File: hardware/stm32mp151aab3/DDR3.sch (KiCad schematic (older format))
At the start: 14 parts

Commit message: update
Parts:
- added C? (x6): 100n, symbol Device:C_Small
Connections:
- net GND: now also C?.2, C?.2, C?.2, C?.2, C?.2, C?.2
- net VDD_DDR: now also C?.1, C?.1, C?.1, C?.1, C?.1, C?.1
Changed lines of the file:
@@
 $Descr A4 11693 8268
 encoding utf-8
-Sheet 6 6
+Sheet 6 7
 Title ""
 Date ""
@@
 Wire Wire Line
 	4350 6600 4350 6800
+Text Label 1350 750  0    50   ~ 0
+DDR_SIGNALS
+$Comp
+L Device:C_Small C?
+U 1 1 6021DB1E
+P 7600 2250
+F 0 "C?" H 7692 2296 50  0000 L CNN
+F 1 "100n" H 7692 2205 50  0000 L CNN
+F 2 "" H 7600 2250 50  0001 C CNN
+F 3 "~" H 7600 2250 50  0001 C CNN
+	1    7600 2250
+	1    0    0    -1
+$EndComp
+$Comp
+L Device:C_Small C?
+U 1 1 6021DB28
+P 8000 2250
+F 0 "C?" H 8092 2296 50  0000 L CNN
+F 1 "100n" H 8092 2205 50  0000 L CNN
+F 2 "" H 8000 2250 50  0001 C CNN
+F 3 "~" H 8000 2250 50  0001 C CNN
+	1    8000 2250
+	1    0    0    -1
+$EndComp
+$Comp
+L Device:C_Small C?
+U 1 1 6021DB32
+P 8400 2250
+F 0 "C?" H 8492 2296 50  0000 L CNN
+F 1 "100n" H 8492 2205 50  0000 L CNN
+F 2 "" H 8400 2250 50  0001 C CNN
+F 3 "~" H 8400 2250 50  0001 C CNN
+	1    8400 2250
+	1    0    0    -1
+$EndComp
+$Comp
+L Device:C_Small C?
+U 1 1 6021DB3C
+P 8800 2250
+F 0 "C?" H 8892 2296 50  0000 L CNN
+F 1 "100n" H 8892 2205 50  0000 L CNN
+F 2 "" H 8800 2250 50  0001 C CNN
+F 3 "~" H 8800 2250 50  0001 C CNN
+	1    8800 2250
+	1    0    0    -1
+$EndComp
+$Comp
+L Device:C_Small C?
+U 1 1 6021DB46
+P 9200 2250
+F 0 "C?" H 9292 2296 50  0000 L CNN
+F 1 "100n" H 9292 2205 50  0000 L CNN
+F 2 "" H 9200 2250 50  0001 C CNN
+F 3 "~" H 9200 2250 50  0001 C CNN
+	1    9200 2250
+	1    0    0    -1
+$EndComp
+$Comp
+L Device:C_Small C?
+U 1 1 6021DB50
+P 9600 2250
+F 0 "C?" H 9692 2296 50  0000 L CNN
+F 1 "100n" H 9692 2205 50  0000 L CNN
+F 2 "" H 9600 2250 50  0001 C CNN
+F 3 "~" H 9600 2250 50  0001 C CNN
+	1    9600 2250
+	1    0    0    -1
+$EndComp
+Wire Wire Line
+	9600 2150 9600 2100
+Wire Wire Line
+	7200 2100 7600 2100
+$Comp
+L power:GND #PWR?
+U 1 1 6021DB5C
+P 7600 2450
+F 0 "#PWR?" H 7600 2200 50  0001 C CNN
+F 1 "GND" H 7605 2277 50  0000 C CNN
+F 2 "" H 7600 2450 50  0001 C CNN
+F 3 "" H 7600 2450 50  0001 C CNN
+	1    7600 2450
+	1    0    0    -1
+$EndComp
+Wire Wire Line
+	7600 2350 7600 2400
+Wire Wire Line
+	7600 2400 8000 2400
+Wire Wire Line
+	9600 2400 9600 2350
+Connection ~ 7600 2400
+Wire Wire Line
+	7600 2400 7600 2450
+Wire Wire Line
+	9200 2350 9200 2400
+Connection ~ 9200 2400
+Wire Wire Line
+	9200 2400 9600 2400
+Wire Wire Line
+	8000 2350 8000 2400
+Connection ~ 8000 2400
+Wire Wire Line
+	8000 2400 8400 2400
+Wire Wire Line
+	8400 2350 8400 2400
+Connection ~ 8400 2400
+Wire Wire Line
+	8400 2400 8800 2400
+Wire Wire Line
+	8800 2350 8800 2400
+Connection ~ 8800 2400
+Wire Wire Line
+	8800 2400 9200 2400
+Wire Wire Line
+	7600 2150 7600 2100
+Connection ~ 7600 2100
+Wire Wire Line
+	7600 2100 8000 2100
+Wire Wire Line
+	8000 2150 8000 2100
+Connection ~ 8000 2100
+Wire Wire Line
+	8000 2100 8400 2100
+Wire Wire Line
+	8400 2150 8400 2100
+Connection ~ 8400 2100
+Wire Wire Line
+	8400 2100 8800 2100
+Wire Wire Line
+	8800 2150 8800 2100
+Connection ~ 8800 2100
+Wire Wire Line
+	8800 2100 9200 2100
+Wire Wire Line
+	9200 2150 9200 2100
+Connection ~ 9200 2100
+Wire Wire Line
+	9200 2100 9600 2100
+Wire Wire Line
+	7200 1450 7200 2100
 Wire Bus Line
 	2000 750  2000 6350
+Connection ~ 7200 1450
 $EndSCHEMATC

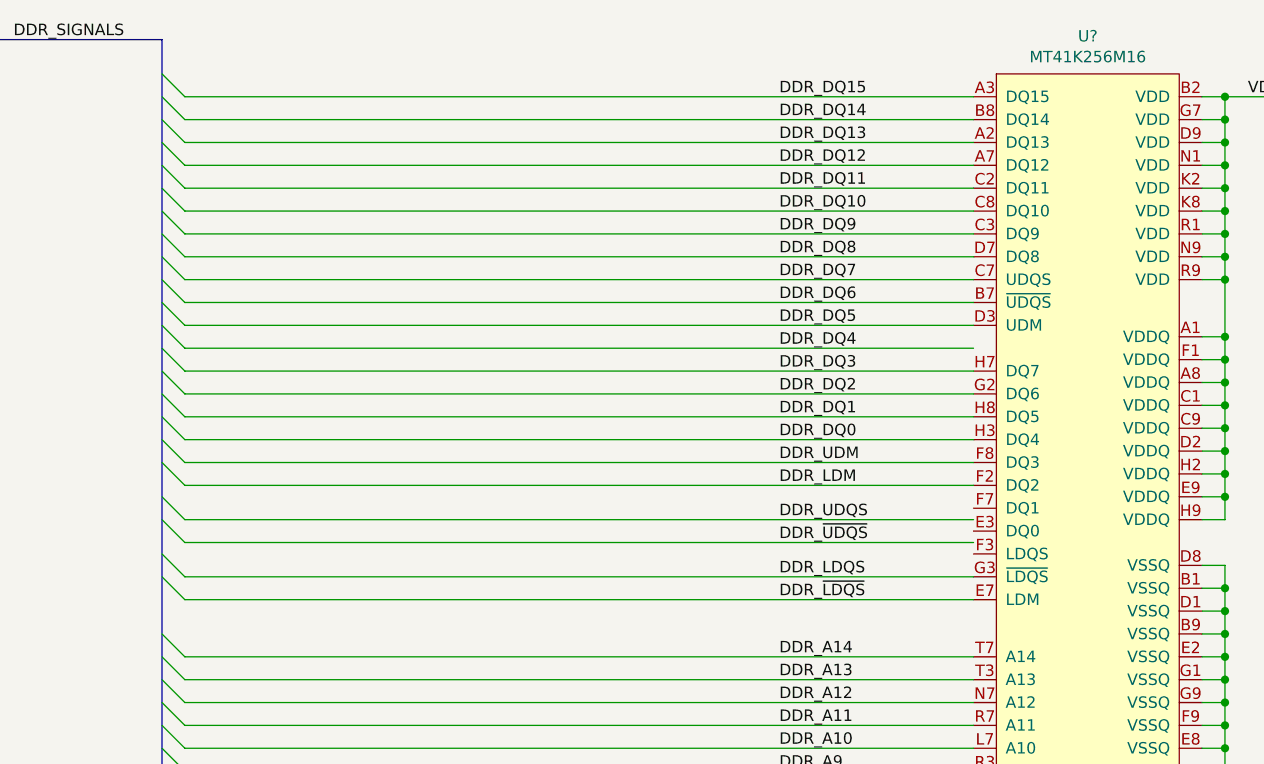
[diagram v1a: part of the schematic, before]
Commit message: update schematic and pdf
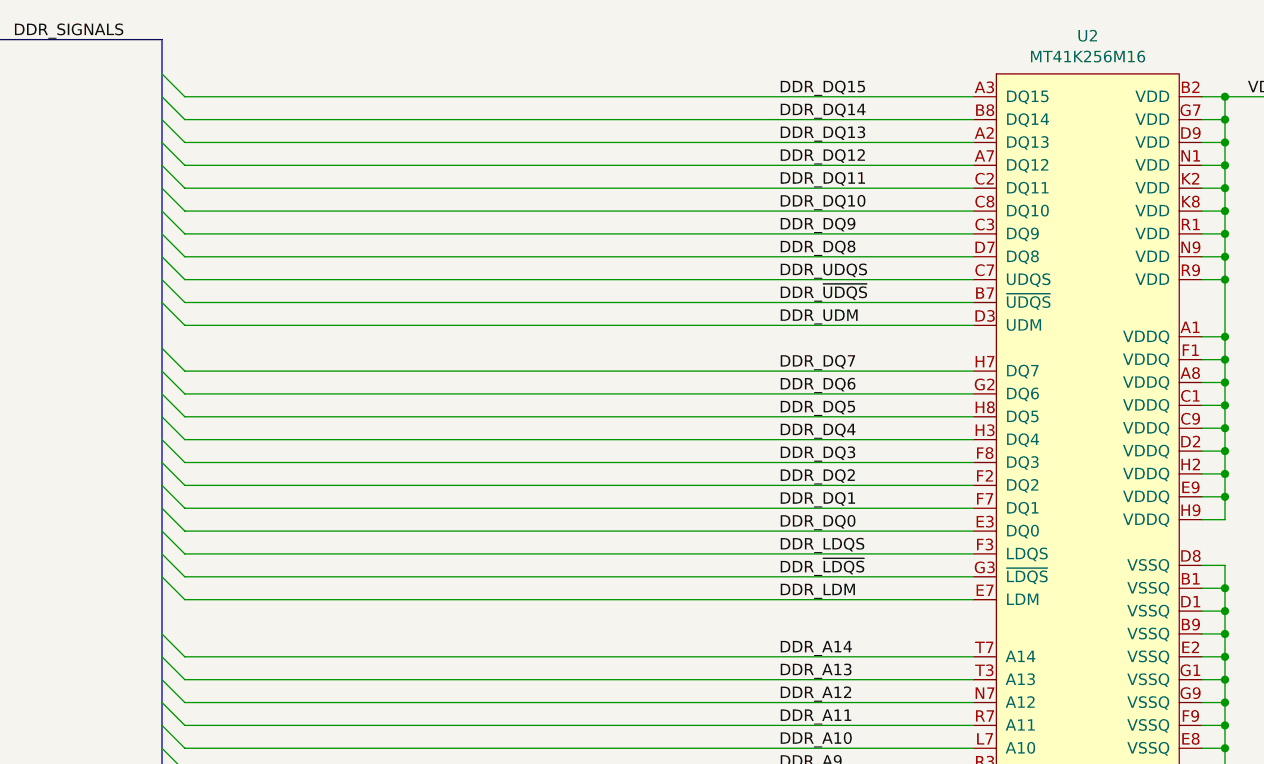
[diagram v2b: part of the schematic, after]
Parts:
- gave numbers to parts that had none: 1
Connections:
- net DDR_DQ0: now also U2.E3 (DQ0); no longer U2.H3 (DQ4)
- net DDR_DQ1: now also U2.F7 (DQ1); no longer U2.H8 (DQ5)
- net DDR_DQ2: now also U2.F2 (DQ2); no longer U2.G2 (DQ6)
- net DDR_DQ3: now also U2.F8 (DQ3); no longer U2.H7 (DQ7)
- net DDR_DQ4: now also U2.H3 (DQ4)
- net DDR_DQ5: now also U2.H8 (DQ5); no longer U2.D3 (UDM)
- net DDR_DQ6: now also U2.G2 (DQ6); no longer U2.B7 (~UDQS)
- net DDR_DQ7: now also U2.H7 (DQ7); no longer U2.C7 (UDQS)
- net DDR_LDM: now also U2.E7 (LDM); no longer U2.F2 (DQ2)
- net DDR_LDQS: now also U2.F3 (LDQS); no longer U2.G3 (~LDQS)
- net DDR_UDM: now also U2.D3 (UDM); no longer U2.F8 (DQ3)
- net DDR_UDQS: now also U2.C7 (UDQS)
- net DDR_~LDQS: now also U2.G3 (~LDQS); no longer U2.E7 (LDM)
- net DDR_~UDQS: now also U2.B7 (~UDQS)
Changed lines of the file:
@@
 $EndDescr
 $Comp
-L stm32mp151:MT41K256M16 U?
+L stm32mp151:MT41K256M16 U2
 U 1 1 5FEB1632
 P 5650 1000
-F 0 "U?" H 6050 1265 50  0000 C CNN
+F 0 "U2" H 6050 1265 50  0000 C CNN
 F 1 "MT41K256M16" H 6050 1174 50  0000 C CNN
 F 2 "" H 6550 -1400 50  0001 C CNN
@@
 Entry Wire Line
 	2000 3100 2100 3200
-Wire Wire Line
-	2100 3200 5550 3200
-Wire Wire Line
-	5550 3100 2100 3100
+Text Label 4700 3000 0    50   ~ 0
+DDR_LDQS
 Text Label 4700 3100 0    50   ~ 0
-DDR_LDQS
-Text Label 4700 3200 0    50   ~ 0
 DDR_~LDQS
 Entry Wire Line
-	2000 2750 2100 2850
-Entry Wire Line
-	2000 2850 2100 2950
-Wire Wire Line
-	2100 2950 5550 2950
-Wire Wire Line
-	5550 2850 2100 2850
-Text Label 4700 2850 0    50   ~ 0
+	2000 2800 2100 2900
+Entry Wire Line
+	2000 2900 2100 3000
+Text Label 4700 1800 0    50   ~ 0
 DDR_UDQS
-Text Label 4700 2950 0    50   ~ 0
+Text Label 4700 1900 0    50   ~ 0
 DDR_~UDQS
 Entry Wire Line
@@
 DDR_A14
 Entry Wire Line
+	2000 2700 2100 2800
+Entry Wire Line
 	2000 2600 2100 2700
+Text Label 4700 3200 0    50   ~ 0
+DDR_LDM
 Entry Wire Line
 	2000 2500 2100 2600
-Wire Wire Line
-	2100 2700 5550 2700
-Wire Wire Line
-	5550 2600 2100 2600
+Entry Wire Line
+	2000 2400 2100 2500
+Entry Wire Line
+	2000 2300 2100 2400
+Entry Wire Line
+	2000 2200 2100 2300
+Entry Wire Line
+	2000 2100 2100 2200
+Entry Wire Line
+	2000 1900 2100 2000
+Entry Wire Line
+	2000 1800 2100 1900
+Entry Wire Line
+	2000 1700 2100 1800
+Entry Wire Line
+	2000 1600 2100 1700
+Entry Wire Line
+	2000 1500 2100 1600
+Entry Wire Line
+	2000 1400 2100 1500
+Entry Wire Line
+	2000 1300 2100 1400
+Entry Wire Line
+	2000 1200 2100 1300
+Entry Wire Line
+	2000 1100 2100 1200
+Entry Wire Line
+	2000 1000 2100 1100
+Entry Wire Line
+	2000 900  2100 1000
+Wire Wire Line
+	2100 1700 5550 1700
+Wire Wire Line
+	5550 1600 2100 1600
+Wire Wire Line
+	2100 1500 5550 1500
+Wire Wire Line
+	5550 1400 2100 1400
+Wire Wire Line
+	2100 1300 5550 1300
+Wire Wire Line
+	5550 1200 2100 1200
+Wire Wire Line
+	2100 1100 5550 1100
+Wire Wire Line
+	5550 1000 2100 1000
+Text Label 4700 2900 0    50   ~ 0
+DDR_DQ0
+Text Label 4700 2800 0    50   ~ 0
+DDR_DQ1
 Text Label 4700 2700 0    50   ~ 0
-DDR_LDM
+DDR_DQ2
 Text Label 4700 2600 0    50   ~ 0
-DDR_UDM
-Entry Wire Line
-	2000 2400 2100 2500
-Entry Wire Line
-	2000 2300 2100 2400
-Entry Wire Line
-	2000 2200 2100 2300
-Entry Wire Line
-	2000 2100 2100 2200
-Entry Wire Line
-	2000 2000 2100 2100
-Entry Wire Line
-	2000 1900 2100 2000
-Entry Wire Line
-	2000 1800 2100 1900
-Entry Wire Line
-	2000 1700 2100 1800
-Entry Wire Line
-	2000 1600 2100 1700
-Entry Wire Line
-	2000 1500 2100 1600
-Entry Wire Line
-	2000 1400 2100 1500
-Entry Wire Line
-	2000 1300 2100 1400
-Entry Wire Line
-	2000 1200 2100 1300
-Entry Wire Line
-	2000 1100 2100 1200
-Entry Wire Line
-	2000 1000 2100 1100
-Entry Wire Line
-	2000 900  2100 1000
-Wire Wire Line
-	2100 2500 5550 2500
-Wire Wire Line
-	5550 2400 2100 2400
-Wire Wire Line
-	2100 2300 5550 2300
-Wire Wire Line
-	2100 2200 5550 2200
-Wire Wire Line
-	2100 2100 5550 2100
-Wire Wire Line
-	5550 2000 2100 2000
-Wire Wire Line
-	2100 1900 5550 1900
-Wire Wire Line
-	5550 1800 2100 1800
-Wire Wire Line
-	2100 1700 5550 1700
-Wire Wire Line
-	5550 1600 2100 1600
-Wire Wire Line
-	2100 1500 5550 1500
-Wire Wire Line
-	5550 1400 2100 1400
-Wire Wire Line
-	2100 1300 5550 1300
-Wire Wire Line
-	5550 1200 2100 1200
-Wire Wire Line
-	2100 1100 5550 1100
-Wire Wire Line
-	5550 1000 2100 1000
+DDR_DQ3
 Text Label 4700 2500 0    50   ~ 0
-DDR_DQ0
+DDR_DQ4
 Text Label 4700 2400 0    50   ~ 0
-DDR_DQ1
+DDR_DQ5
 Text Label 4700 2300 0    50   ~ 0
-DDR_DQ2
+DDR_DQ6
 Text Label 4700 2200 0    50   ~ 0
-DDR_DQ3
-Text Label 4700 2100 0    50   ~ 0
-DDR_DQ4
-Text Label 4700 2000 0    50   ~ 0
-DDR_DQ5
-Text Label 4700 1900 0    50   ~ 0
-DDR_DQ6
-Text Label 4700 1800 0    50   ~ 0
 DDR_DQ7
 Text Label 4700 1700 0    50   ~ 0
@@
 Wire Wire Line
 	7200 1450 7200 2100
+Connection ~ 7200 1450
+Text Label 4700 2000 0    50   ~ 0
+DDR_UDM
+Wire Wire Line
+	5550 3200 2100 3200
+Wire Wire Line
+	5550 2600 2100 2600
+Wire Wire Line
+	5550 2200 2100 2200
+Wire Wire Line
+	2100 2300 5550 2300
+Wire Wire Line
+	5550 2400 2100 2400
+Wire Wire Line
+	5550 1800 2100 1800
+Wire Wire Line
+	2100 1900 5550 1900
+Wire Wire Line
+	5550 2000 2100 2000
+Wire Wire Line
+	2100 2500 5550 2500
+Wire Wire Line
+	5550 3100 2100 3100
+Wire Wire Line
+	2100 3000 5550 3000
+Wire Wire Line
+	5550 2900 2100 2900
+Wire Wire Line
+	2100 2800 5550 2800
+Wire Wire Line
+	5550 2700 2100 2700
 Wire Bus Line
 	2000 750  2000 6350
-Connection ~ 7200 1450
 $EndSCHEMATC
